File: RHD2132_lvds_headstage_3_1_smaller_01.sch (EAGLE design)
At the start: 13 parts, among them U1 RHD2132_QFN

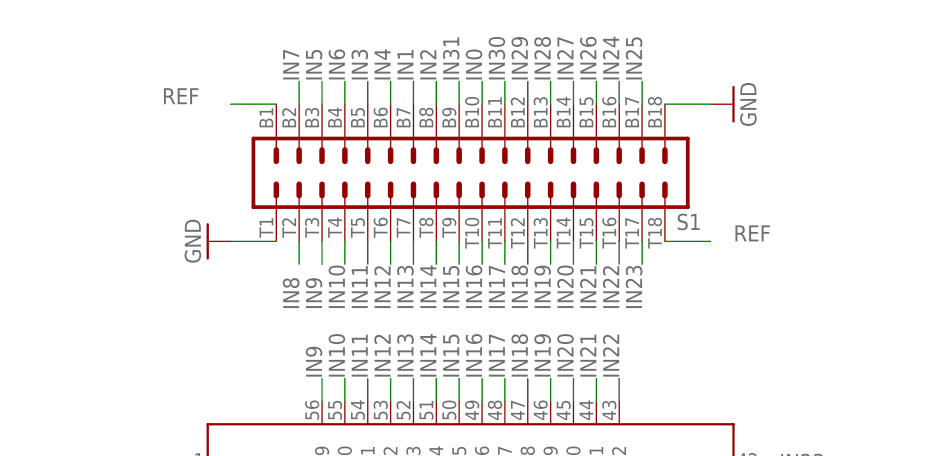
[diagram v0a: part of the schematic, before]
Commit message: made gnd/ref pinout plexon etc compatible
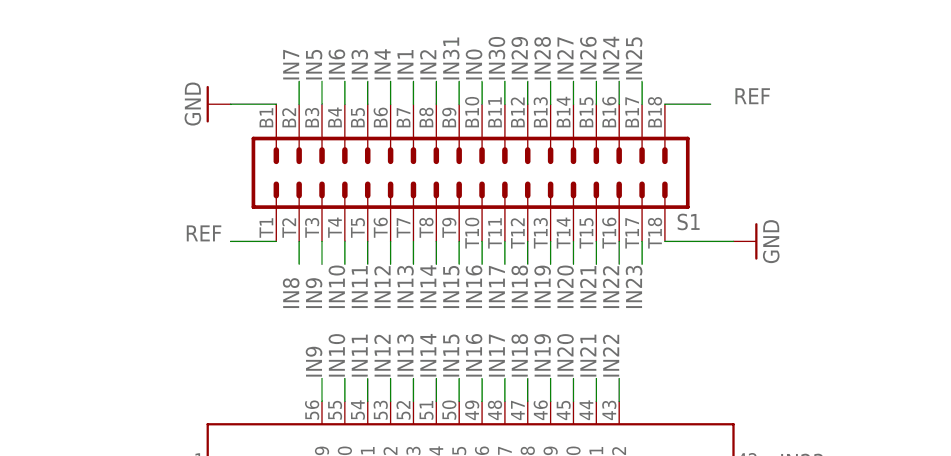
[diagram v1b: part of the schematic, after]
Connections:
- net GND: now also S1.B1, S1.T18; no longer S1.B18, S1.T1
- net REF: now also S1.B18, S1.T1; no longer S1.B1, S1.T18
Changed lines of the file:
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@@
 <?xml version="1.0" encoding="utf-8"?>
 <!DOCTYPE eagle SYSTEM "eagle.dtd">
-<eagle version="6.1">
+<eagle version="6.3">
 <drawing>
 <settings>
@@
 <instance part="GND14" gate="1" x="-15.24" y="-38.1"/>
 <instance part="GND15" gate="1" x="-86.36" y="-60.96" rot="R270"/>
-<instance part="GND16" gate="1" x="-27.94" y="50.8" rot="R270"/>
-<instance part="GND17" gate="1" x="30.48" y="66.04" rot="R90"/>
+<instance part="GND16" gate="1" x="-27.94" y="66.04" rot="R270"/>
+<instance part="GND17" gate="1" x="33.02" y="50.8" rot="R90"/>
 </instances>
 <busses>
@@
 <nets>
 <net name="GND" class="0">
-<segment>
-<pinref part="S1" gate="A" pin="B18"/>
-<wire x1="22.86" y1="66.04" x2="27.94" y2="66.04" width="0.1524" layer="91"/>
-<pinref part="GND17" gate="1" pin="GND"/>
-</segment>
-<segment>
-<pinref part="S1" gate="A" pin="T1"/>
-<wire x1="-20.32" y1="50.8" x2="-25.4" y2="50.8" width="0.1524" layer="91"/>
-<pinref part="GND16" gate="1" pin="GND"/>
-</segment>
 <segment>
 <wire x1="27.94" y1="-83.82" x2="27.94" y2="-73.66" width="0.1524" layer="91"/>
@@
 <wire x1="-78.74" y1="-60.96" x2="-83.82" y2="-60.96" width="0.1524" layer="91"/>
 </segment>
+<segment>
+<pinref part="GND16" gate="1" pin="GND"/>
+<pinref part="S1" gate="A" pin="B1"/>
+<wire x1="-25.4" y1="66.04" x2="-20.32" y2="66.04" width="0.1524" layer="91"/>
+</segment>
+<segment>
+<pinref part="GND17" gate="1" pin="GND"/>
+<pinref part="S1" gate="A" pin="T18"/>
+<wire x1="30.48" y1="50.8" x2="22.86" y2="50.8" width="0.1524" layer="91"/>
+</segment>
 </net>
 <net name="REF" class="0">
-<segment>
-<pinref part="S1" gate="A" pin="B1"/>
-<wire x1="-20.32" y1="66.04" x2="-25.4" y2="66.04" width="0.1524" layer="91"/>
-<label x="-33.02" y="66.04" size="1.778" layer="95"/>
-</segment>
-<segment>
-<pinref part="S1" gate="A" pin="T18"/>
-<wire x1="22.86" y1="50.8" x2="27.94" y2="50.8" width="0.1524" layer="91"/>
-<label x="30.48" y="50.8" size="1.778" layer="95"/>
-</segment>
 <segment>
 <pinref part="U1" gate="A" pin="REF_ELEC"/>
@@
 <label x="-40.64" y="0" size="1.778" layer="95"/>
 </segment>
+<segment>
+<pinref part="S1" gate="A" pin="T1"/>
+<wire x1="-20.32" y1="50.8" x2="-25.4" y2="50.8" width="0.1524" layer="91"/>
+<label x="-30.48" y="50.8" size="1.778" layer="95"/>
+</segment>
+<segment>
+<pinref part="S1" gate="A" pin="B18"/>
+<wire x1="22.86" y1="66.04" x2="27.94" y2="66.04" width="0.1524" layer="91"/>
+<label x="30.48" y="66.04" size="1.778" layer="95"/>
+</segment>
 </net>
